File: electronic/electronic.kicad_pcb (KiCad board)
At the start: 2 copper layers, 68 x 75 mm, 20 parts, among them J1 POWER SUPLY, J25 Conn_01x05, J26 Conn_01x04, J27 Conn_01x04, J28 Conn_01x05, J3 M01, J4 ENC01, J5 M02, J6 ENC02, J8 M03, J9 ENC03, U1 ESP32-S3-DevKitC

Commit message: chore: PCB updated
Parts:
- moved J28 52.5 mm to (21.5, 54.0)
- moved J25 3.52 mm to (29.5, 54.0)
- moved J27 2.18 mm to (75.5, 60.0)
- moved J5 2.18 mm to (75.5, 42.0)
- moved J8 2.18 mm to (75.5, 51.0)
- moved J26 2.18 mm to (75.5, 28.2)
- moved J3 2.18 mm to (74.5, 22.0)
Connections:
- U1 pad 10: unconnected-(U1-GPIO17/ADC2_CH6-Pad10) -> DRVI102
- U1 pad 11: unconnected-(U1-GPIO18/ADC2_CH7-Pad11) -> DRVI202
- U1 pad 40: DRVI202 -> unconnected-(U1-GPIO2/ADC1_CH1-Pad40)
- U1 pad 41: DRVI102 -> unconnected-(U1-GPIO1/ADC1_CH0-Pad41)
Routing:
- net DRVI102: track 9.20 -> 19.8 mm
- net DRVI202: track 9.22 -> 19.3 mm
- net DRVI301: track 11.5 -> 7.86 mm
- net DRVI401: track 11.5 -> 7.87 mm
- net DRVI201: track 11.6 -> 8.21 mm
- net DRVI101: track 11.6 -> 8.23 mm

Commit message: chore: PCB updated
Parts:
- added J29: Screw_Terminal_01x03, Connector_JST:JST_XH_B3B-XH-A_1x03_P2.50mm_Vertical, F.Cu at (68.0, 46.0)
- added J30: Screw_Terminal_01x03, Connector_JST:JST_XH_B3B-XH-A_1x03_P2.50mm_Vertical, F.Cu at (68.0, 34.0)
- moved J26 0.50 mm to (76.0, 28.2)
- moved J27 0.50 mm to (76.0, 60.0)
- moved J3 0.50 mm to (75.0, 22.0)
- moved J5 0.50 mm to (76.0, 42.0)
- moved J8 0.50 mm to (76.0, 51.0)
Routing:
- net +5V: track 0.00 -> 104.3 mm
- net +12V: track 0.00 -> 42.4 mm

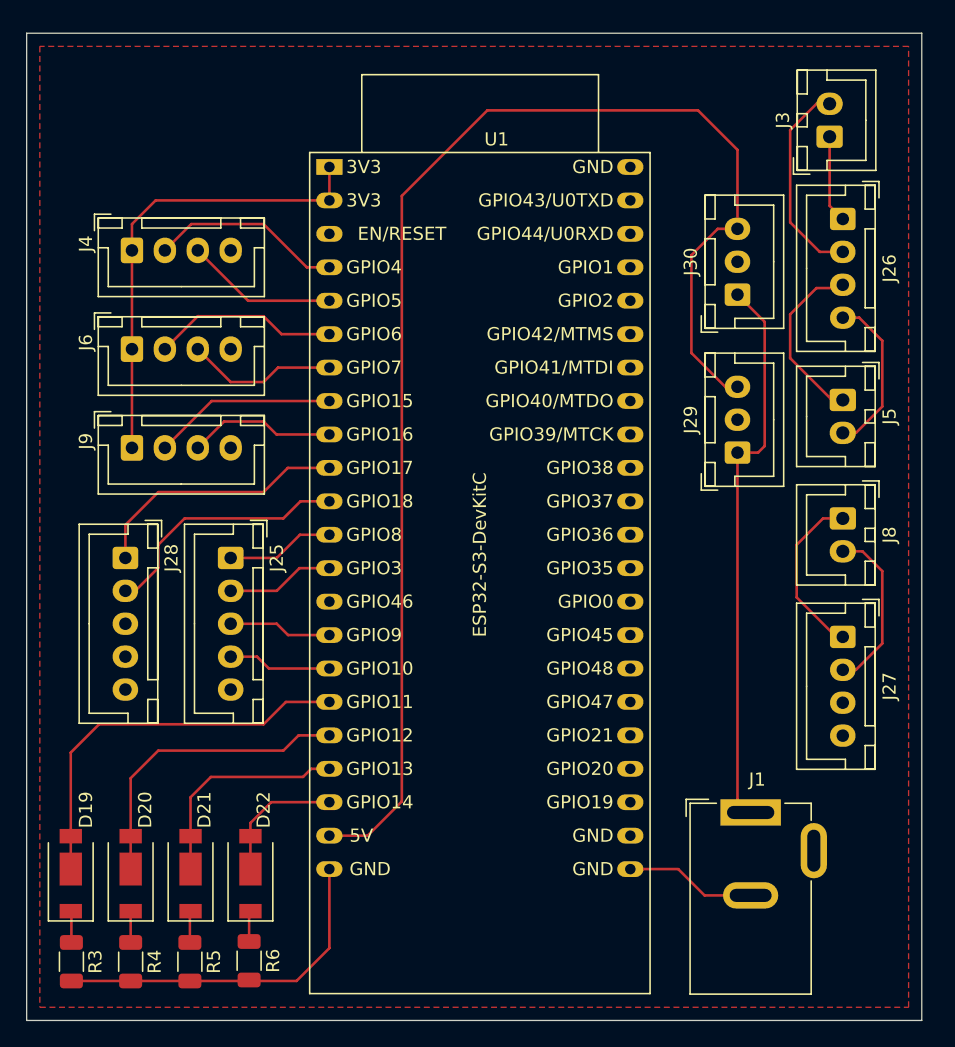
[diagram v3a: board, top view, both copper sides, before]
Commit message: chore: M3 hole added to PCB
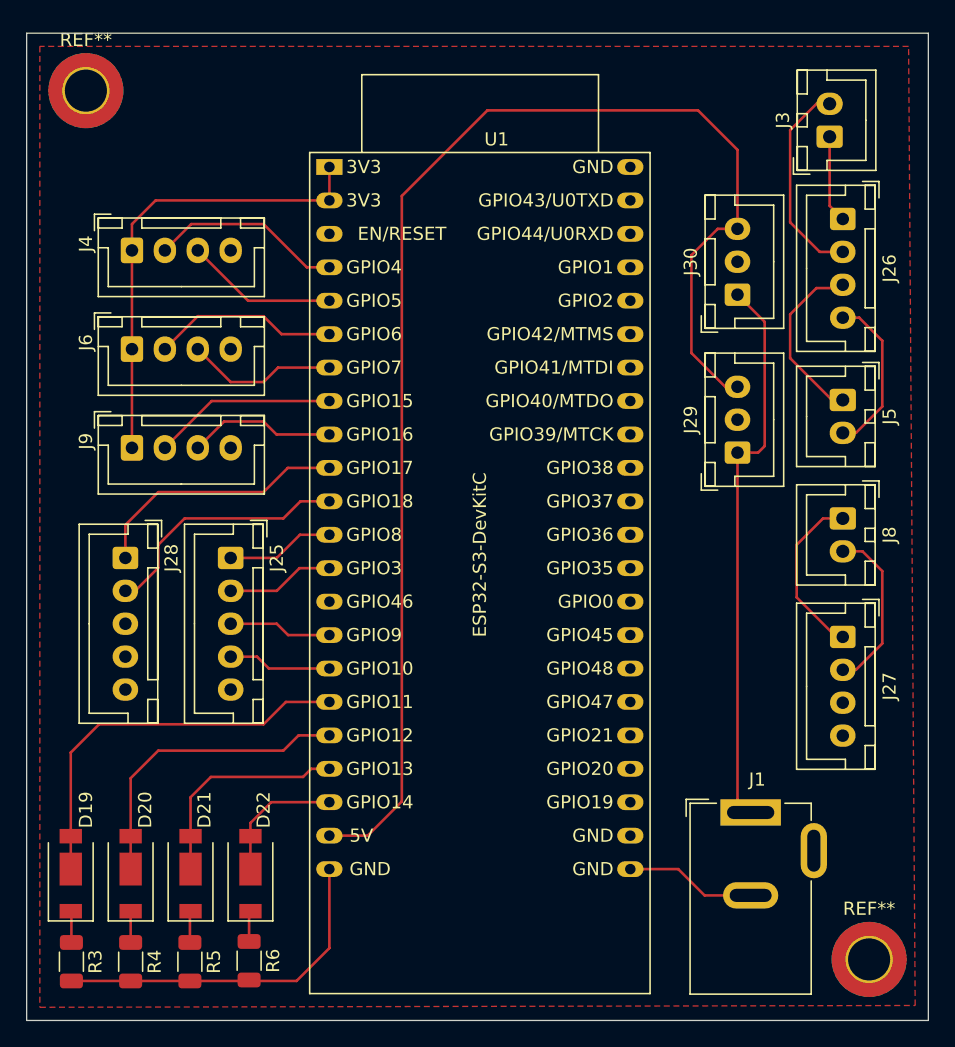
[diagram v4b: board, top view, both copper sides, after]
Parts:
- added REF**: MountingHole_3.2mm_M3_ISO7380_Pad_TopBottom, MountingHole:MountingHole_3.2mm_M3_ISO7380_Pad_TopBottom, F.Cu at (78.0, 84.5)
- added REF**: MountingHole_3.2mm_M3_ISO7380_Pad_TopBottom, MountingHole:MountingHole_3.2mm_M3_ISO7380_Pad_TopBottom, F.Cu at (18.5, 18.5)
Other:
- board size 68 x 75 mm -> 68.5 x 75 mm
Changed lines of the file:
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@@
 		)
+	)
+	(footprint "MountingHole:MountingHole_3.2mm_M3_ISO7380_Pad_TopBottom"
+		(layer "F.Cu")
+		(at 78 84.5)
+		(descr "Mounting Hole 3.2mm, M3, ISO7380")
+		(tags "mounting hole 3.2mm m3 iso7380")
+		(property "Reference" "REF**"
+			(at 0 -3.85 0)
+			(layer "F.SilkS")
+			(effects
+				(font
+					(size 1 1)
+					(thickness 0.15)
+				)
+			)
+		)
+		(property "Value" "MountingHole_3.2mm_M3_ISO7380_Pad_TopBottom"
+			(at 0 3.85 0)
+			(layer "F.Fab")
+			(hide yes)
+			(effects
+				(font
+					(size 1 1)
+					(thickness 0.15)
+				)
+			)
+		)
+		(property "Datasheet" ""
+			(at 0 0 0)
+			(unlocked yes)
+			(layer "F.Fab")
+			(hide yes)
+			(effects
+				(font
+					(size 1.27 1.27)
+					(thickness 0.15)
+				)
+			)
+		)
+		(property "Description" ""
+			(at 0 0 0)
+			(unlocked yes)
+			(layer "F.Fab")
+			(hide yes)
+			(effects
+				(font
+					(size 1.27 1.27)
+					(thickness 0.15)
+				)
+			)
+		)
+		(attr exclude_from_pos_files exclude_from_bom)
+		(fp_circle
+			(center 0 0)
+			(end 2.85 0)
+			(stroke
+				(width 0.15)
+				(type solid)
+			)
+			(fill no)
+			(layer "Cmts.User")
+		)
+		(fp_circle
+			(center 0 0)
+			(end 3.1 0)
+			(stroke
+				(width 0.05)
+				(type solid)
+			)
+			(fill no)
+			(layer "F.CrtYd")
+		)
+		(fp_text user "${REFERENCE}"
+			(at 0 0 0)
+			(layer "F.Fab")
+			(effects
+				(font
+					(size 1 1)
+					(thickness 0.15)
+				)
+			)
+		)
+		(pad "1" thru_hole circle
+			(at 0 0)
+			(size 3.6 3.6)
+			(drill 3.2)
+			(layers "*.Cu" "*.Mask")
+			(remove_unused_layers no)
+		)
+		(pad "1" connect circle
+			(at 0 0)
+			(size 5.7 5.7)
+			(layers "F.Cu" "F.Mask")
+		)
+		(pad "1" connect circle
+			(at 0 0)
+			(size 5.7 5.7)
+			(layers "B.Cu" "B.Mask")
+		)
+		(embedded_fonts no)
 	)
 	(footprint "Resistor_SMD:R_1206_3216Metric"
@@
 		)
 	)
+	(footprint "MountingHole:MountingHole_3.2mm_M3_ISO7380_Pad_TopBottom"
+		(layer "F.Cu")
+		(at 18.5 18.5)
+		(descr "Mounting Hole 3.2mm, M3, ISO7380")
+		(tags "mounting hole 3.2mm m3 iso7380")
+		(property "Reference" "REF**"
+			(at 0 -3.85 0)
+			(layer "F.SilkS")
+			(effects
+				(font
+					(size 1 1)
+					(thickness 0.15)
+				)
+			)
+		)
+		(property "Value" "MountingHole_3.2mm_M3_ISO7380_Pad_TopBottom"
+			(at 0 3.85 0)
+			(layer "F.Fab")
+			(hide yes)
+			(effects
+				(font
+					(size 1 1)
+					(thickness 0.15)
+				)
+			)
+		)
+		(property "Datasheet" ""
+			(at 0 0 0)
+			(unlocked yes)
+			(layer "F.Fab")
+			(hide yes)
+			(effects
+				(font
+					(size 1.27 1.27)
+					(thickness 0.15)
+				)
+			)
+		)
+		(property "Description" ""
+			(at 0 0 0)
+			(unlocked yes)
+			(layer "F.Fab")
+			(hide yes)
+			(effects
+				(font
+					(size 1.27 1.27)
+					(thickness 0.15)
+				)
+			)
+		)
+		(attr exclude_from_pos_files exclude_from_bom)
+		(fp_circle
+			(center 0 0)
+			(end 2.85 0)
+			(stroke
+				(width 0.15)
+				(type solid)
+			)
+			(fill no)
+			(layer "Cmts.User")
+		)
+		(fp_circle
+			(center 0 0)
+			(end 3.1 0)
+			(stroke
+				(width 0.05)
+				(type solid)
+			)
+			(fill no)
+			(layer "F.CrtYd")
+		)
+		(fp_text user "${REFERENCE}"
+			(at 0 0 0)
+			(layer "F.Fab")
+			(effects
+				(font
+					(size 1 1)
+					(thickness 0.15)
+				)
+			)
+		)
+		(pad "1" thru_hole circle
+			(at 0 0)
+			(size 3.6 3.6)
+			(drill 3.2)
+			(layers "*.Cu" "*.Mask")
+			(remove_unused_layers no)
+		)
+		(pad "1" connect circle
+			(at 0 0)
+			(size 5.7 5.7)
+			(layers "F.Cu" "F.Mask")
+		)
+		(pad "1" connect circle
+			(at 0 0)
+			(size 5.7 5.7)
+			(layers "B.Cu" "B.Mask")
+		)
+		(embedded_fonts no)
+	)
 	(footprint "Connector_JST:JST_XH_B2B-XH-A_1x02_P2.50mm_Vertical"
 		(layer "F.Cu")
@@
 	(gr_rect
 		(start 14 14.13728)
-		(end 82 89.13728)
+		(end 82.5 89.13728)
 		(stroke
 			(width 0.05)
@@
 		(polygon
 			(pts
-				(xy 15 15.13728) (xy 15 88.13728) (xy 81 88.13728) (xy 81 15.13728)
-			)
-		)
+				(xy 15 15.13728) (xy 15 88.13728) (xy 81.5 88) (xy 81 15.13728)
+			)
+		)
